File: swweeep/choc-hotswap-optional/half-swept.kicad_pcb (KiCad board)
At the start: 2 copper layers, 113.3 x 89.7 mm, 34 parts, among them J1 JST-BATTERY, SW1 SW_Push, SW10 SW_Push, SW11 SW_Push, SW12 SW_Push, SW14 SW_Push, SW15 SW_Push, SW16 SW_Push, SW17 SW_Push, SW18 SW_Push, SW2 SW_Push, SW20 SW_Push, SW21 SW_Push, SW3 SW_Push, SW4 SW_Push, SW5 SW_Push, SW6 SW_Push, SW7 SW_DPDT, SW8 SW_Push, SW9 SW_Push, U1 nice_nano

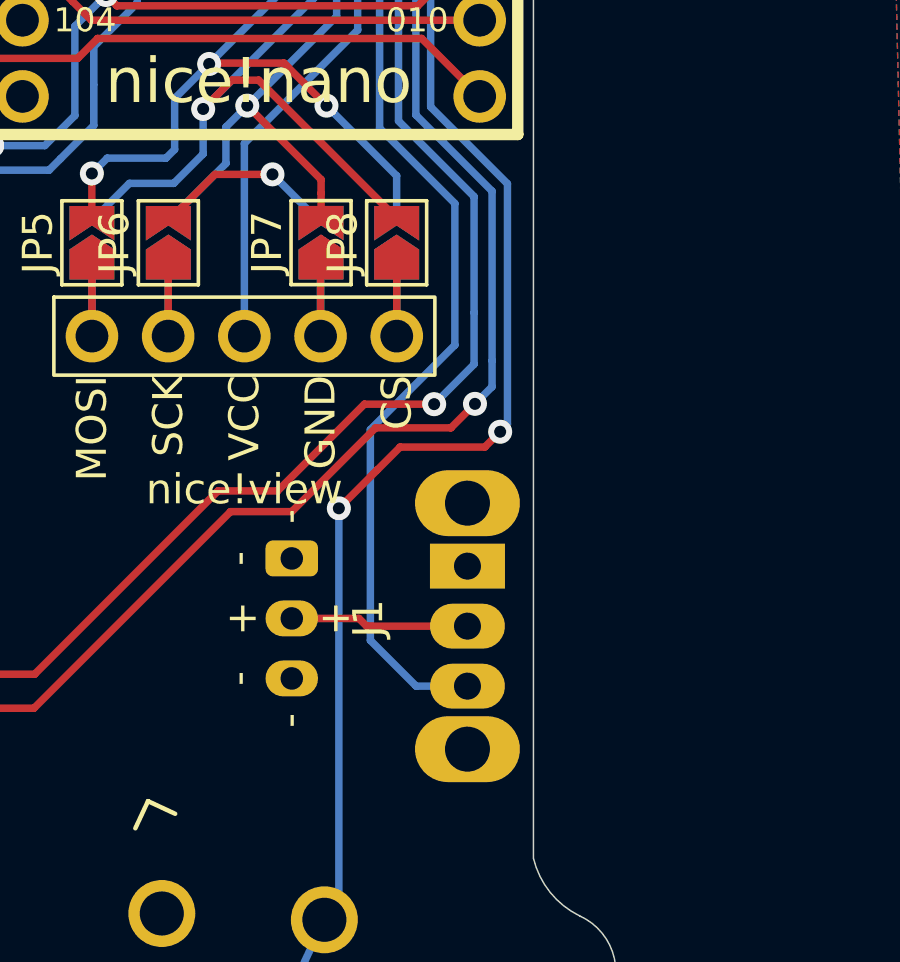
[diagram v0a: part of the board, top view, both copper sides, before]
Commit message: Revert "replaced on off switch, from MSK12C02 to OS102011MA1QN1"
This reverts commit 761ca253cc3f7c0a016fc91ec44eaa0a86f70d5a.
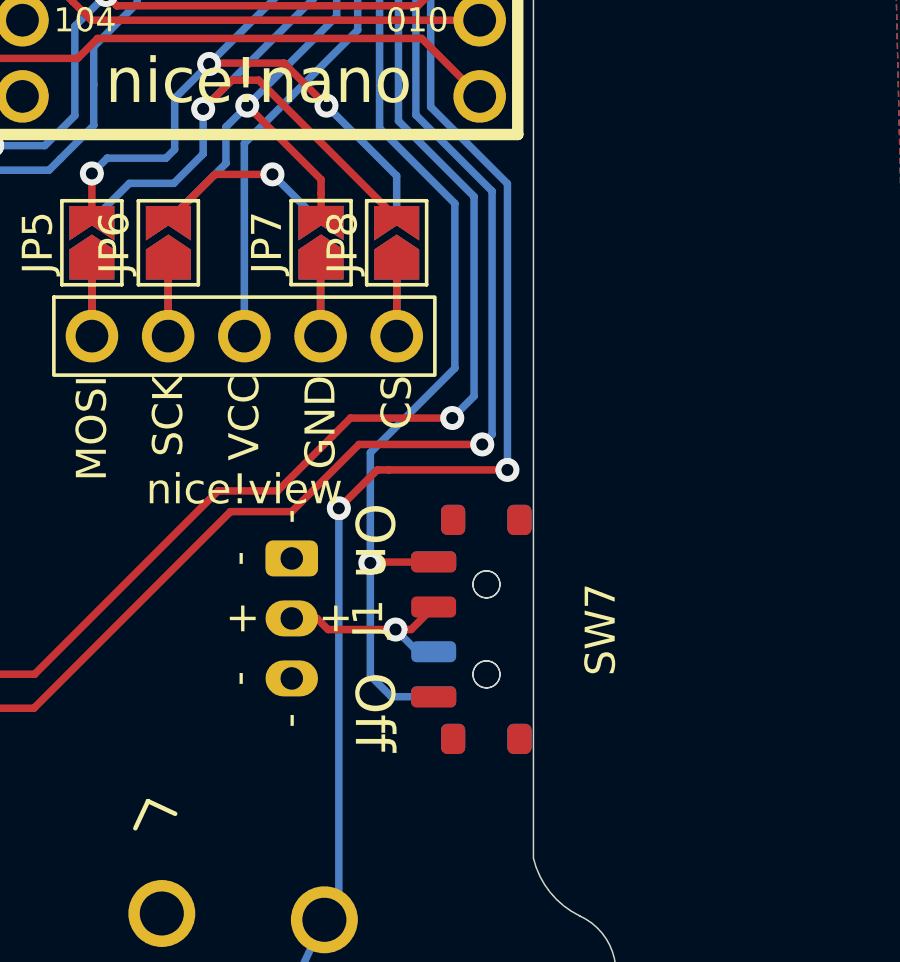
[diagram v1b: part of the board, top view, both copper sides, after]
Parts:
- added SW13: SW_DPDT, fingerpunch:MSK-12C02, B.Cu at (121.2, 75.7)
- SW7: footprint fingerpunch:SW_CuK_OS102011MA1QN1_SPDT_Angled -> fingerpunch:MSK-12C02; moved to F.Cu
- moved SW7 2.21 mm to (121.2, 75.7)
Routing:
- net raw: track 55.4 -> 57.2 mm, vias 1 -> 2
- net gnd: track 31.6 -> 32.6 mm
- net Switch17: track 76.7 -> 77.6 mm
- net Switch16: track 66.5 -> 67.4 mm
- net Net-(J1-Pad2): track 5.96 -> 6.77 mm, vias 0 -> 1
- net Switch18: track 99.2 -> 99.8 mm

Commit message: added ferris
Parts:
- added G***: LOGO, copper_pads:ferris, F.Cu at (54.6, 78.5)
- added G***: LOGO, copper_pads:ferris_sweep, B.Cu at (56.0, 76.8)
